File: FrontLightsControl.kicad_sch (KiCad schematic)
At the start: 0 parts

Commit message: added output driver
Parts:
- added U10, U11, U12, U13, U3, U5, U6, U7, U8, U9: VND7050AJTR, easyeda2kicad:POWERSSO-16_L4.9-W3.9-P0.50-LS6.0-BL-EP, symbol easyeda2kicad:VND7050AJTR
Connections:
- new net +12V: U10.17 (VCC), U11.17 (VCC), U12.17 (VCC), U13.17 (VCC), U3.17 (VCC), U5.17 (VCC), U6.17 (VCC), U7.17 (VCC), U8.17 (VCC), U9.17 (VCC)
- new net Load0: U3.13 (OUTPUT0), U3.14 (OUTPUT0), U3.15 (OUTPUT0), U3.16 (OUTPUT0)
- new net Load1: U3.10 (OUTPUT1), U3.11 (OUTPUT1), U3.12 (OUTPUT1), U3.9 (OUTPUT1)
- new net Load10: U11.13 (OUTPUT0), U11.14 (OUTPUT0), U11.15 (OUTPUT0), U11.16 (OUTPUT0)
- new net Load11: U11.10 (OUTPUT1), U11.11 (OUTPUT1), U11.12 (OUTPUT1), U11.9 (OUTPUT1)
- new net Load12: U12.13 (OUTPUT0), U12.14 (OUTPUT0), U12.15 (OUTPUT0), U12.16 (OUTPUT0)
- new net Load13: U12.10 (OUTPUT1), U12.11 (OUTPUT1), U12.12 (OUTPUT1), U12.9 (OUTPUT1)
- new net Load14: U13.13 (OUTPUT0), U13.14 (OUTPUT0), U13.15 (OUTPUT0), U13.16 (OUTPUT0)
- new net Load15: U13.10 (OUTPUT1), U13.11 (OUTPUT1), U13.12 (OUTPUT1), U13.9 (OUTPUT1)
- new net Load16: U9.13 (OUTPUT0), U9.14 (OUTPUT0), U9.15 (OUTPUT0), U9.16 (OUTPUT0)
- new net Load17: U9.10 (OUTPUT1), U9.11 (OUTPUT1), U9.12 (OUTPUT1), U9.9 (OUTPUT1)
- new net Load18: U10.13 (OUTPUT0), U10.14 (OUTPUT0), U10.15 (OUTPUT0), U10.16 (OUTPUT0)
- new net Load19: U10.10 (OUTPUT1), U10.11 (OUTPUT1), U10.12 (OUTPUT1), U10.9 (OUTPUT1)
- new net Load2: U5.13 (OUTPUT0), U5.14 (OUTPUT0), U5.15 (OUTPUT0), U5.16 (OUTPUT0)
- new net Load3: U5.10 (OUTPUT1), U5.11 (OUTPUT1), U5.12 (OUTPUT1), U5.9 (OUTPUT1)
- new net Load4: U6.13 (OUTPUT0), U6.14 (OUTPUT0), U6.15 (OUTPUT0), U6.16 (OUTPUT0)
- new net Load5: U6.10 (OUTPUT1), U6.11 (OUTPUT1), U6.12 (OUTPUT1), U6.9 (OUTPUT1)
- new net Load6: U7.13 (OUTPUT0), U7.14 (OUTPUT0), U7.15 (OUTPUT0), U7.16 (OUTPUT0)
- new net Load7: U7.10 (OUTPUT1), U7.11 (OUTPUT1), U7.12 (OUTPUT1), U7.9 (OUTPUT1)
- new net Load8: U8.13 (OUTPUT0), U8.14 (OUTPUT0), U8.15 (OUTPUT0), U8.16 (OUTPUT0)
- new net Load9: U8.10 (OUTPUT1), U8.11 (OUTPUT1), U8.12 (OUTPUT1), U8.9 (OUTPUT1)

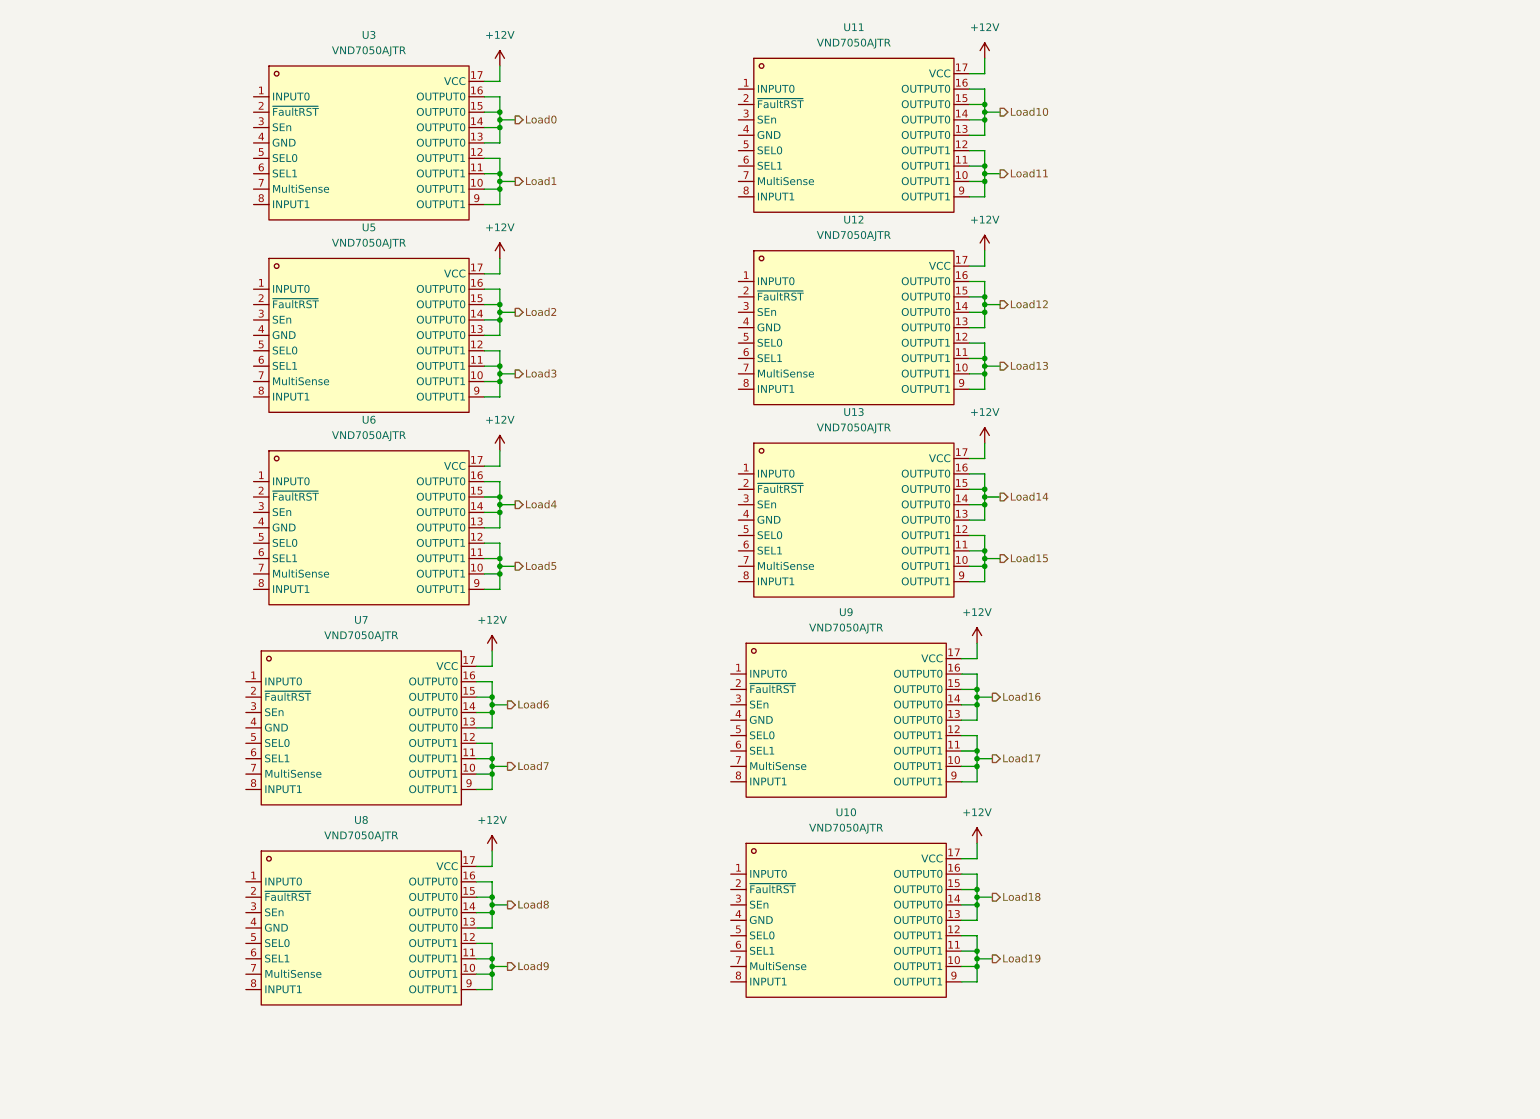
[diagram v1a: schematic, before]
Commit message: added schematic for input (switch, PAS, analog) + output
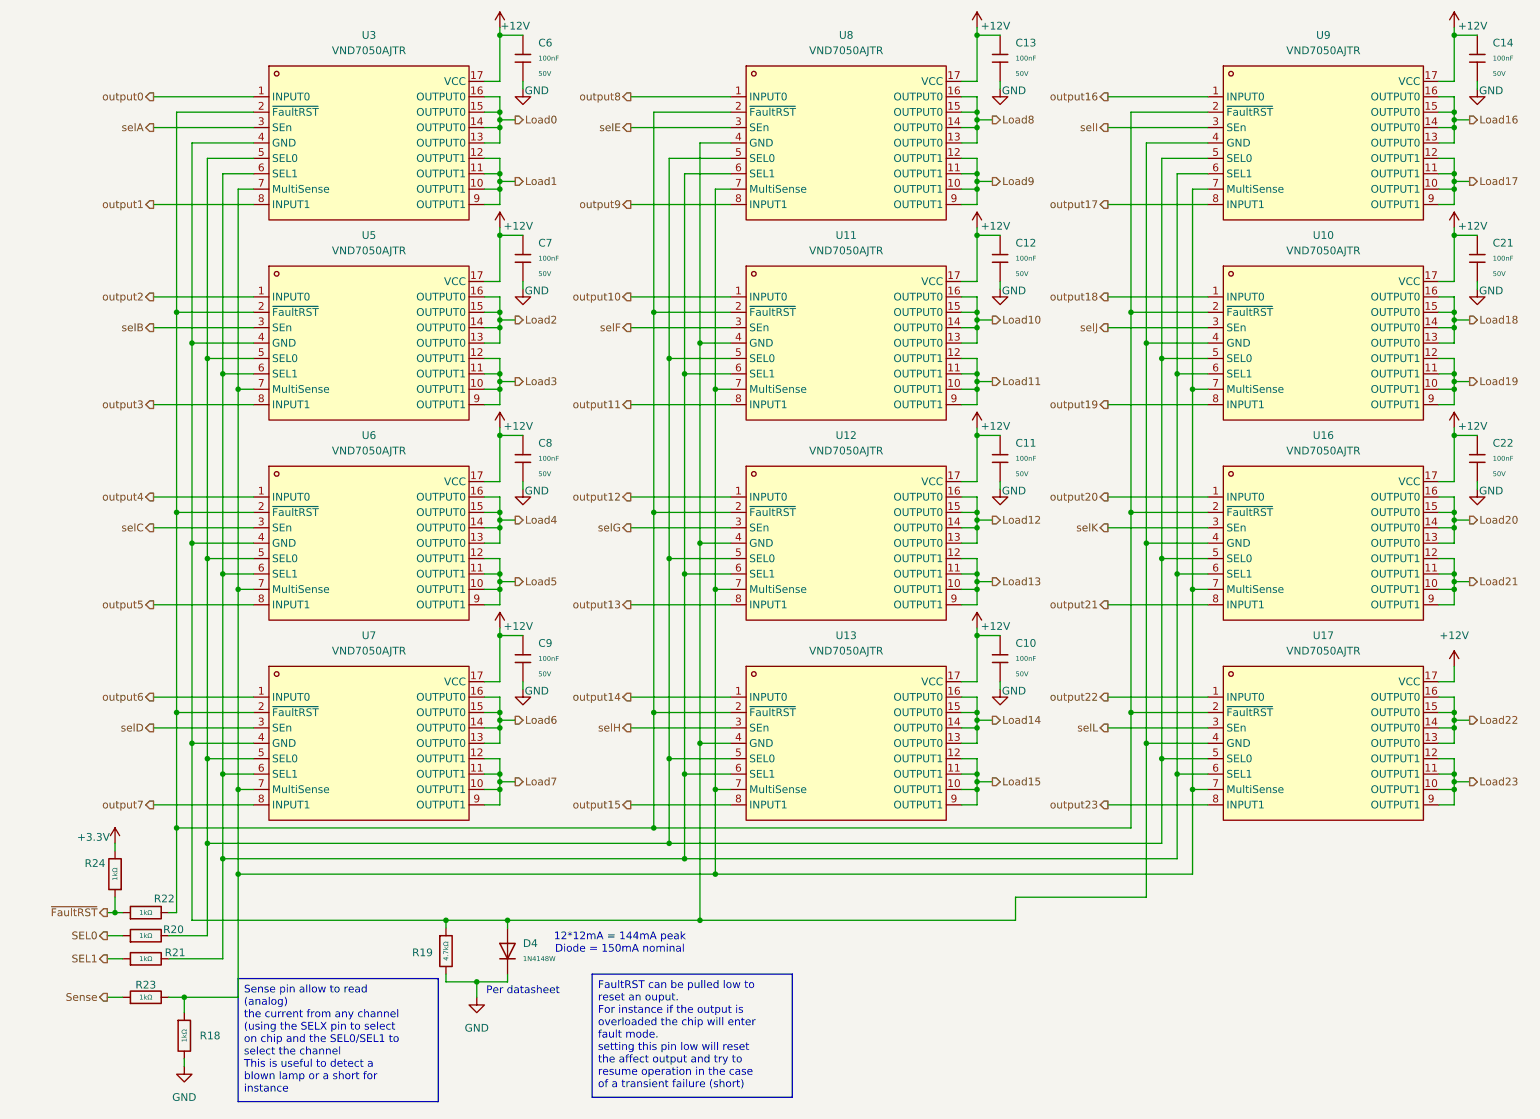
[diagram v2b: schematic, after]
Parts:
- added C10, C11, C12, C13, C14, C21, C22, C6, C7, C8, C9: 100nF, PCM_JLCPCB:C_0805, symbol PCM_JLCPCB-Capacitors:0805,100nF,(2)
- added D4: 1N4148W, PCM_JLCPCB:D_SOD-123, symbol PCM_JLCPCB-Diodes:Switching,1N4148W
- added R18, R20, R21, R22, R23, R24: 1kΩ, PCM_JLCPCB:R_0805, symbol PCM_JLCPCB-Resistors:0805,1kΩ
- added R19: 4.7kΩ, PCM_JLCPCB:R_0805, symbol PCM_JLCPCB-Resistors:0805,4.7kΩ
- added U16, U17: VND7050AJTR, easyeda2kicad:POWERSSO-16_L4.9-W3.9-P0.50-LS6.0-BL-EP, symbol easyeda2kicad:VND7050AJTR
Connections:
- net +12V: now also C10.1, C11.1, C12.1, C13.1, C14.1, C21.1, C22.1, C6.1, C7.1, C8.1, C9.1, U16.17 (VCC), U17.17 (VCC)
- net output0: now reaches U3.1 (INPUT0)
- net at U3.2 (~{FaultRST}): now also U10.2 (~{FaultRST}), U11.2 (~{FaultRST}), U12.2 (~{FaultRST}), U13.2 (~{FaultRST}), U5.2 (~{FaultRST}), U6.2 (~{FaultRST}), U7.2 (~{FaultRST}), U8.2 (~{FaultRST}), U9.2 (~{FaultRST}), R22.2, U16.2 (~{FaultRST}), U17.2 (~{FaultRST})
- net selA: now reaches U3.3 (SEn)
- net at U3.4 (GND): now also U10.4 (GND), U11.4 (GND), U12.4 (GND), U13.4 (GND), U5.4 (GND), U6.4 (GND), U7.4 (GND), U8.4 (GND), U9.4 (GND), D4.2, R19.1, U16.4 (GND), U17.4 (GND)
- net at U3.5 (SEL0): now also U10.5 (SEL0), U11.5 (SEL0), U12.5 (SEL0), U13.5 (SEL0), U5.5 (SEL0), U6.5 (SEL0), U7.5 (SEL0), U8.5 (SEL0), U9.5 (SEL0), R20.2, U16.5 (SEL0), U17.5 (SEL0)
- net at U3.6 (SEL1): now also U10.6 (SEL1), U11.6 (SEL1), U12.6 (SEL1), U13.6 (SEL1), U5.6 (SEL1), U6.6 (SEL1), U7.6 (SEL1), U8.6 (SEL1), U9.6 (SEL1), R21.2, U16.6 (SEL1), U17.6 (SEL1)
- net at U3.7 (MultiSense): now also U10.7 (MultiSense), U11.7 (MultiSense), U12.7 (MultiSense), U13.7 (MultiSense), U5.7 (MultiSense), U6.7 (MultiSense), U7.7 (MultiSense), U8.7 (MultiSense), U9.7 (MultiSense), R18.1, R23.2, U16.7 (MultiSense), U17.7 (MultiSense)
- net output1: now reaches U3.8 (INPUT1)
- net output8: now reaches U8.1 (INPUT0)
- net selE: now reaches U8.3 (SEn)
- net output9: now reaches U8.8 (INPUT1)
- net output12: now reaches U12.1 (INPUT0)
- net selG: now reaches U12.3 (SEn)
- net output13: now reaches U12.8 (INPUT1)
- net output4: now reaches U6.1 (INPUT0)
- net selC: now reaches U6.3 (SEn)
- net output5: now reaches U6.8 (INPUT1)
- net output2: now reaches U5.1 (INPUT0)
- net selB: now reaches U5.3 (SEn)
- net output3: now reaches U5.8 (INPUT1)
- net output14: now reaches U13.1 (INPUT0)
- net selH: now reaches U13.3 (SEn)
- net output15: now reaches U13.8 (INPUT1)
- net output18: now reaches U10.1 (INPUT0)
- net selJ: now reaches U10.3 (SEn)
- net output19: now reaches U10.8 (INPUT1)
- net output10: now reaches U11.1 (INPUT0)
- net selF: now reaches U11.3 (SEn)
- net output11: now reaches U11.8 (INPUT1)
- net output6: now reaches U7.1 (INPUT0)
- net selD: now reaches U7.3 (SEn)
- net output7: now reaches U7.8 (INPUT1)
- net output16: now reaches U9.1 (INPUT0)
- net selI: now reaches U9.3 (SEn)
- net output17: now reaches U9.8 (INPUT1)
- new net +3.3V: R24.2
- new net GND: C10.2, C11.2, C12.2, C13.2, C14.2, C21.2, C22.2, C6.2, C7.2, C8.2, C9.2, D4.1, R18.2, R19.2
- new net Load20: U16.13 (OUTPUT0), U16.14 (OUTPUT0), U16.15 (OUTPUT0), U16.16 (OUTPUT0)
- new net Load21: U16.10 (OUTPUT1), U16.11 (OUTPUT1), U16.12 (OUTPUT1), U16.9 (OUTPUT1)
- new net Load22: U17.13 (OUTPUT0), U17.14 (OUTPUT0), U17.15 (OUTPUT0), U17.16 (OUTPUT0)
- new net Load23: U17.10 (OUTPUT1), U17.11 (OUTPUT1), U17.12 (OUTPUT1), U17.9 (OUTPUT1)
- new net SEL0: R20.1
- new net SEL1: R21.1
- new net Sense: R23.1
- new net output20: U16.1 (INPUT0)
- new net output21: U16.8 (INPUT1)
- new net output22: U17.1 (INPUT0)
- new net output23: U17.8 (INPUT1)
- new net selK: U16.3 (SEn)
- new net selL: U17.3 (SEn)
- new net ~{FaultRST}: R22.1, R24.1
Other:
- note added: "12*12mA = 144mA peak Diode = 150mA nominal"
- note added: "Per datasheet"
- moved on the sheet: U10, U11, U12, U13, U5, U6, U7, U8, U9

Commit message: wiring MCU to input and ouput
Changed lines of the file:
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@@
 		)
 	)
-	(text_box "FaultRST can be pulled low to reset an ouput.\nFor instance if the output is overloaded the chip will enter fault mode.\nsetting this pin low will reset the affect output and try to resume operation in the case of a transient failure (short)\n"
+	(text_box "FaultRST can be pulled low to reset an ouput.\nIf the output is overloaded the chip will enter fault mode.\nsetting this pin low will reset the affect output and try to resume operation in the case of a transient failure (short)\n"
 		(exclude_from_sim no)
 		(at 102.87 176.53 0)
@@
 	)
 	(hierarchical_label "output2"
-		(shape output)
+		(shape input)
 		(at 30.48 64.77 180)
 		(effects
@@
 	)
 	(hierarchical_label "output23"
-		(shape output)
+		(shape input)
 		(at 187.96 148.59 180)
 		(effects
@@
 	)
 	(hierarchical_label "selE"
-		(shape output)
+		(shape input)
 		(at 109.22 36.83 180)
 		(effects
@@
 	)
 	(hierarchical_label "selH"
-		(shape output)
+		(shape input)
 		(at 109.22 135.89 180)
 		(effects
@@
 	)
 	(hierarchical_label "output10"
-		(shape output)
+		(shape input)
 		(at 109.22 64.77 180)
 		(effects
@@
 	)
 	(hierarchical_label "output1"
-		(shape output)
+		(shape input)
 		(at 30.48 49.53 180)
 		(effects
@@
 	)
 	(hierarchical_label "output19"
-		(shape output)
+		(shape input)
 		(at 187.96 82.55 180)
 		(effects
@@
 	)
 	(hierarchical_label "SEL1"
-		(shape output)
+		(shape input)
 		(at 22.86 173.99 180)
 		(effects
@@
 	)
 	(hierarchical_label "output18"
-		(shape output)
+		(shape input)
 		(at 187.96 64.77 180)
 		(effects
@@
 	)
 	(hierarchical_label "selG"
-		(shape output)
+		(shape input)
 		(at 109.22 102.87 180)
 		(effects
@@
 	)
 	(hierarchical_label "selI"
-		(shape output)
+		(shape input)
 		(at 187.96 36.83 180)
 		(effects
@@
 	)
 	(hierarchical_label "~{FaultRST}"
-		(shape output)
+		(shape input)
 		(at 22.86 166.37 180)
 		(effects
@@
 	)
 	(hierarchical_label "output20"
-		(shape output)
+		(shape input)
 		(at 187.96 97.79 180)
 		(effects
@@
 	)
 	(hierarchical_label "output5"
-		(shape output)
+		(shape input)
 		(at 30.48 115.57 180)
 		(effects
@@
 	)
 	(hierarchical_label "output16"
-		(shape output)
+		(shape input)
 		(at 187.96 31.75 180)
 		(effects
@@
 	)
 	(hierarchical_label "selA"
-		(shape output)
+		(shape input)
 		(at 30.48 36.83 180)
 		(effects
@@
 	)
 	(hierarchical_label "output14"
-		(shape output)
+		(shape input)
 		(at 109.22 130.81 180)
 		(effects
@@
 	)
 	(hierarchical_label "selK"
-		(shape output)
+		(shape input)
 		(at 187.96 102.87 180)
 		(effects
@@
 	)
 	(hierarchical_label "output8"
-		(shape output)
+		(shape input)
 		(at 109.22 31.75 180)
 		(effects
@@
 	)
 	(hierarchical_label "selJ"
-		(shape output)
+		(shape input)
 		(at 187.96 69.85 180)
 		(effects
@@
 	)
 	(hierarchical_label "selF"
-		(shape output)
+		(shape input)
 		(at 109.22 69.85 180)
 		(effects
@@
 	)
 	(hierarchical_label "output9"
-		(shape output)
+		(shape input)
 		(at 109.22 49.53 180)
 		(effects
@@
 	)
 	(hierarchical_label "output21"
-		(shape output)
+		(shape input)
 		(at 187.96 115.57 180)
 		(effects
@@
 	)
 	(hierarchical_label "output15"
-		(shape output)
+		(shape input)
 		(at 109.22 148.59 180)
 		(effects
@@
 	)
 	(hierarchical_label "selC"
-		(shape output)
+		(shape input)
 		(at 30.48 102.87 180)
 		(effects
@@
 	)
 	(hierarchical_label "output17"
-		(shape output)
+		(shape input)
 		(at 187.96 49.53 180)
 		(effects
@@
 	)
 	(hierarchical_label "output11"
-		(shape output)
+		(shape input)
 		(at 109.22 82.55 180)
 		(effects
@@
 	)
 	(hierarchical_label "output22"
-		(shape output)
+		(shape input)
 		(at 187.96 130.81 180)
 		(effects
@@
 	)
 	(hierarchical_label "output7"
-		(shape output)
+		(shape input)
 		(at 30.48 148.59 180)
 		(effects
@@
 	)
 	(hierarchical_label "output3"
-		(shape output)
+		(shape input)
 		(at 30.48 82.55 180)
 		(effects
@@
 	)
 	(hierarchical_label "output4"
-		(shape output)
+		(shape input)
 		(at 30.48 97.79 180)
 		(effects
@@
 	)
 	(hierarchical_label "SEL0"
-		(shape output)
+		(shape input)
 		(at 22.86 170.18 180)
 		(effects
@@
 	)
 	(hierarchical_label "output0"
-		(shape output)
+		(shape input)
 		(at 30.48 31.75 180)
 		(effects
@@
 	)
 	(hierarchical_label "output13"
-		(shape output)
+		(shape input)
 		(at 109.22 115.57 180)
 		(effects
@@
 	)
 	(hierarchical_label "selB"
-		(shape output)
+		(shape input)
 		(at 30.48 69.85 180)
 		(effects
@@
 	)
 	(hierarchical_label "selL"
-		(shape output)
+		(shape input)
 		(at 187.96 135.89 180)
 		(effects
@@
 	)
 	(hierarchical_label "output12"
-		(shape output)
+		(shape input)
 		(at 109.22 97.79 180)
 		(effects
@@
 	)
 	(hierarchical_label "output6"
-		(shape output)
+		(shape input)
 		(at 30.48 130.81 180)
 		(effects
@@
 	)
 	(hierarchical_label "selD"
-		(shape output)
+		(shape input)
 		(at 30.48 135.89 180)
 		(effects

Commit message: started pin assignement
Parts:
- added D1: BAT54S_C7420333, PCM_JLCPCB:SOT-23-3_L2.9-W1.3-P1.90-LS2.4-BR, symbol PCM_JLCPCB-Diode-Packages:Schottky, BAT54S_C7420333
- renumbered C6 to C47, C7 to C48, C8 to C49, C9 to C50, C13 to C51, C12 to C52, C11 to C53, C10 to C54, C14 to C55, C21 to C56, C22 to C57, D4 to D2, R24 to R26, R22 to R27, R20 to R28, R21 to R29, R23 to R30, R18 to R31, R19 to R32, U13 to U10, U9 to U11, U10 to U12, U16 to U13, U17 to U14, U5 to U4, U6 to U5, U7 to U6, U8 to U7, U11 to U8, U12 to U9
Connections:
- net +3.3V: now also D1.2 (K2)
- net GND: now also D1.1 (K1)
- net Sense: now also D1.3 (A)
